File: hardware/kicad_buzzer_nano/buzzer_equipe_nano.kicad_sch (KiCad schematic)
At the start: 8 parts, among them J1 Conn_01x08, J2 Conn_01x04, J3 Conn_01x03, SW1 SW_Push, SW2 SW_SPST

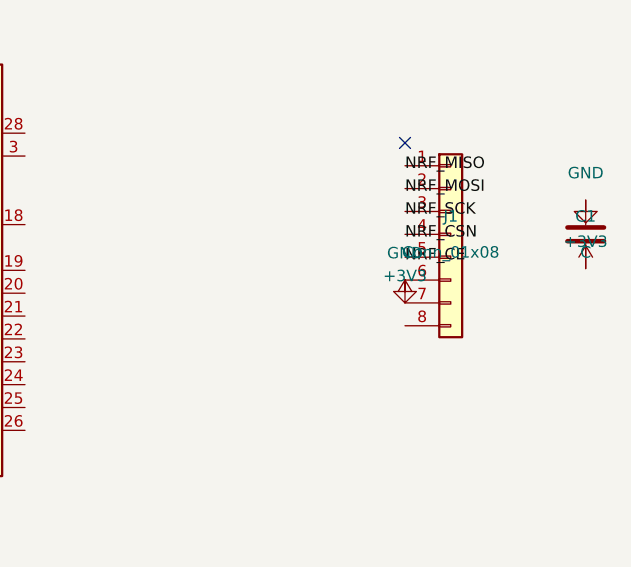
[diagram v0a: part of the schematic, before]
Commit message: hardware: corrige VCC/GND nRF24 (inverses) + passe en 2x4 (module PA+LNA)
En reponse a "le nrf24 c'est sur une ligne ?", verification du brochage
nRF24 contre 3 sources independantes (components101.com,
lastminuteengineers.com, doc generale nRF24L01+) : la broche 1 est GND et
la broche 2 est VCC, pas l'inverse comme c'etait cable jusqu'ici sur J1
(carte Nano) et J_NRF (carte hub) -- schema ET PCB. Broche 1 = toujours la
pastille carree sur cette empreinte, coherent avec "GND identifiable par
son marquage carre" documente pour ce module.

Le module confirme etant un nRF24L01+PA+LNA (longue portee), son connecteur
est 2x4 et non 1x8 standard -- empreinte changee vers PinSocket_2x04 sur
les 2 cartes concernees, brochage 1=GND 2=VCC puis CE/CSN/SCK/MOSI/MISO/IRQ
sur les rangees suivantes (ordre le plus courant publie, mais AUCUN
standard universel n'existe pour les variantes PA+LNA -- avertissement
explicite dans le README et sur la serigraphie: verifier sur le module
recu avant de souder).

Schemas re-verifies (kicad-cli sch erc, memes comptes qu'avant -- aucune
regression). PCB re-routes (Freerouting) et revalides (kicad-cli pcb drc):
0 violation de clearance, 0 element non connecte, 0 track_dangling.

Co-Authored-By: Claude Sonnet 5 <noreply@anthropic.com>
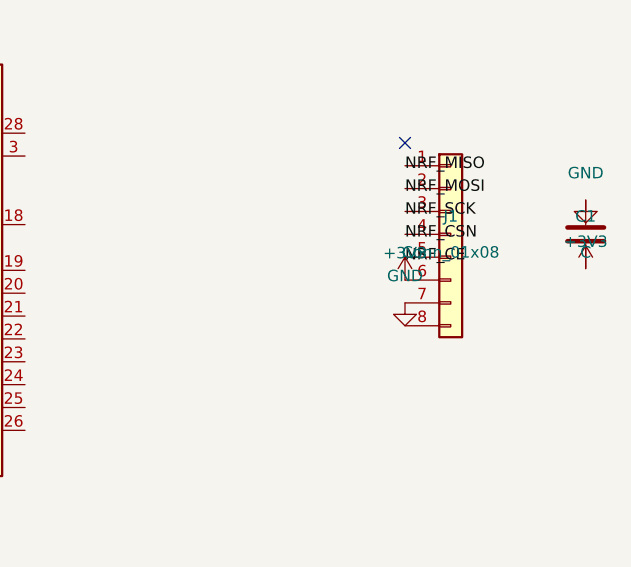
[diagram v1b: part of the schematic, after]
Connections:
- net +3V3: now also J1.6 (Pin_6); no longer J1.7 (Pin_7)
- net GND: now also J1.7 (Pin_7); no longer J1.6 (Pin_6)
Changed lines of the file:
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@@
     (instances
       (project "buzzer_equipe_nano"
-        (path "/182d6f10-6833-4238-9812-46fc12f81c81"
+        (path "/5cdc0e7d-5af0-4908-bc28-46bf68370e45"
           (reference "A1")
           (unit 1)
@@
     (instances
       (project "buzzer_equipe_nano"
-        (path "/182d6f10-6833-4238-9812-46fc12f81c81"
+        (path "/5cdc0e7d-5af0-4908-bc28-46bf68370e45"
           (reference "J1")
           (unit 1)
@@
     (instances
       (project "buzzer_equipe_nano"
-        (path "/182d6f10-6833-4238-9812-46fc12f81c81"
+        (path "/5cdc0e7d-5af0-4908-bc28-46bf68370e45"
           (reference "C1")
           (unit 1)
@@
     (instances
       (project "buzzer_equipe_nano"
-        (path "/182d6f10-6833-4238-9812-46fc12f81c81"
+        (path "/5cdc0e7d-5af0-4908-bc28-46bf68370e45"
           (reference "SW1")
           (unit 1)
@@
     (instances
       (project "buzzer_equipe_nano"
-        (path "/182d6f10-6833-4238-9812-46fc12f81c81"
+        (path "/5cdc0e7d-5af0-4908-bc28-46bf68370e45"
           (reference "J2")
           (unit 1)
@@
     (instances
       (project "buzzer_equipe_nano"
-        (path "/182d6f10-6833-4238-9812-46fc12f81c81"
+        (path "/5cdc0e7d-5af0-4908-bc28-46bf68370e45"
           (reference "BT1")
           (unit 1)
@@
     (instances
       (project "buzzer_equipe_nano"
-        (path "/182d6f10-6833-4238-9812-46fc12f81c81"
+        (path "/5cdc0e7d-5af0-4908-bc28-46bf68370e45"
           (reference "SW2")
           (unit 1)
@@
     (instances
       (project "buzzer_equipe_nano"
-        (path "/182d6f10-6833-4238-9812-46fc12f81c81"
+        (path "/5cdc0e7d-5af0-4908-bc28-46bf68370e45"
           (reference "J3")
           (unit 1)
@@
     (instances
       (project "buzzer_equipe_nano"
-        (path "/182d6f10-6833-4238-9812-46fc12f81c81"
+        (path "/5cdc0e7d-5af0-4908-bc28-46bf68370e45"
           (reference "#PWRGND00")
           (unit 1)
@@
   (symbol
     (lib_id "power:GND")
-    (at 184.92 101.08 0)
+    (at 184.92 103.62 0)
     (unit 1)
     (exclude_from_sim no)
@@
     (dnp no)
     (property "Reference" "#PWRGND01"
-      (at 184.92 96.08 0)
+      (at 184.92 98.62 0)
       (effects (font (size 1.27 1.27)) hide)
     )
     (property "Value" "GND"
-      (at 184.92 98.08 0)
-      (effects (font (size 1.27 1.27)))
-    )
-    (property "Footprint" ""
-      (at 184.92 101.08 0)
-      (effects (font (size 1.27 1.27)) hide)
-    )
-    (property "Datasheet" "~"
-      (at 184.92 101.08 0)
-      (effects (font (size 1.27 1.27)) hide)
-    )
-    (property "Description" ""
-      (at 184.92 101.08 0)
-      (effects (font (size 1.27 1.27)) hide)
-    )
-      (pin "1"
-      )
-    (instances
-      (project "buzzer_equipe_nano"
-        (path "/182d6f10-6833-4238-9812-46fc12f81c81"
+      (at 184.92 100.62 0)
+      (effects (font (size 1.27 1.27)))
+    )
+    (property "Footprint" ""
+      (at 184.92 103.62 0)
+      (effects (font (size 1.27 1.27)) hide)
+    )
+    (property "Datasheet" "~"
+      (at 184.92 103.62 0)
+      (effects (font (size 1.27 1.27)) hide)
+    )
+    (property "Description" ""
+      (at 184.92 103.62 0)
+      (effects (font (size 1.27 1.27)) hide)
+    )
+      (pin "1"
+      )
+    (instances
+      (project "buzzer_equipe_nano"
+        (path "/5cdc0e7d-5af0-4908-bc28-46bf68370e45"
           (reference "#PWRGND01")
           (unit 1)
@@
     (instances
       (project "buzzer_equipe_nano"
-        (path "/182d6f10-6833-4238-9812-46fc12f81c81"
+        (path "/5cdc0e7d-5af0-4908-bc28-46bf68370e45"
           (reference "#PWRGND02")
           (unit 1)
@@
     (instances
       (project "buzzer_equipe_nano"
-        (path "/182d6f10-6833-4238-9812-46fc12f81c81"
+        (path "/5cdc0e7d-5af0-4908-bc28-46bf68370e45"
           (reference "#PWRGND03")
           (unit 1)
@@
     (instances
       (project "buzzer_equipe_nano"
-        (path "/182d6f10-6833-4238-9812-46fc12f81c81"
+        (path "/5cdc0e7d-5af0-4908-bc28-46bf68370e45"
           (reference "#PWRGND04")
           (unit 1)
@@
     (instances
       (project "buzzer_equipe_nano"
-        (path "/182d6f10-6833-4238-9812-46fc12f81c81"
+        (path "/5cdc0e7d-5af0-4908-bc28-46bf68370e45"
           (reference "#PWRGND05")
           (unit 1)
@@
     (instances
       (project "buzzer_equipe_nano"
-        (path "/182d6f10-6833-4238-9812-46fc12f81c81"
+        (path "/5cdc0e7d-5af0-4908-bc28-46bf68370e45"
           (reference "#PWRGND06")
           (unit 1)
@@
     (instances
       (project "buzzer_equipe_nano"
-        (path "/182d6f10-6833-4238-9812-46fc12f81c81"
+        (path "/5cdc0e7d-5af0-4908-bc28-46bf68370e45"
           (reference "#PWRGND07")
           (unit 1)
@@
     (instances
       (project "buzzer_equipe_nano"
-        (path "/182d6f10-6833-4238-9812-46fc12f81c81"
+        (path "/5cdc0e7d-5af0-4908-bc28-46bf68370e45"
           (reference "#PWR3V00")
           (unit 1)
@@
   (symbol
     (lib_id "power:+3V3")
-    (at 184.92 103.62 0)
+    (at 184.92 101.08 0)
     (unit 1)
     (exclude_from_sim no)
@@
     (dnp no)
     (property "Reference" "#PWR3V01"
-      (at 184.92 98.62 0)
+      (at 184.92 96.08 0)
       (effects (font (size 1.27 1.27)) hide)
     )
     (property "Value" "+3V3"
-      (at 184.92 100.62 0)
-      (effects (font (size 1.27 1.27)))
-    )
-    (property "Footprint" ""
-      (at 184.92 103.62 0)
-      (effects (font (size 1.27 1.27)) hide)
-    )
-    (property "Datasheet" "~"
-      (at 184.92 103.62 0)
-      (effects (font (size 1.27 1.27)) hide)
-    )
-    (property "Description" ""
-      (at 184.92 103.62 0)
-      (effects (font (size 1.27 1.27)) hide)
-    )
-      (pin "1"
-      )
-    (instances
-      (project "buzzer_equipe_nano"
-        (path "/182d6f10-6833-4238-9812-46fc12f81c81"
+      (at 184.92 98.08 0)
+      (effects (font (size 1.27 1.27)))
+    )
+    (property "Footprint" ""
+      (at 184.92 101.08 0)
+      (effects (font (size 1.27 1.27)) hide)
+    )
+    (property "Datasheet" "~"
+      (at 184.92 101.08 0)
+      (effects (font (size 1.27 1.27)) hide)
+    )
+    (property "Description" ""
+      (at 184.92 101.08 0)
+      (effects (font (size 1.27 1.27)) hide)
+    )
+      (pin "1"
+      )
+    (instances
+      (project "buzzer_equipe_nano"
+        (path "/5cdc0e7d-5af0-4908-bc28-46bf68370e45"
           (reference "#PWR3V01")
           (unit 1)
@@
     (instances
       (project "buzzer_equipe_nano"
-        (path "/182d6f10-6833-4238-9812-46fc12f81c81"
+        (path "/5cdc0e7d-5af0-4908-bc28-46bf68370e45"
           (reference "#PWR3V02")
           (unit 1)
